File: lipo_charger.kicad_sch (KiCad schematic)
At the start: 19 parts, among them J1 USB_B_Micro, J2 22-23-2021, Q1 2N7002DW-7-F, SW1 SW_SPDT, U1 MCP73831, U2 DIO6605B, U3 AP9101CK

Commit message: Create footprint for boost IC and reroute
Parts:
- U2: footprint Package_DFN_QFN:DFN-8-1EP_3x2mm_P0.5mm_EP1.7x1.4mm -> Package_DFN_QFN:DFN-8-1EP_3x2mm_P0.5mm_EP1.6x1.5mm
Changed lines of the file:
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@@
     (property "Reference" "U2" (id 0) (at 81.28 113.03 0))
     (property "Value" "DIO6605B" (id 1) (at 81.28 115.57 0))
-    (property "Footprint" "Package_DFN_QFN:DFN-8-1EP_3x2mm_P0.5mm_EP1.7x1.4mm" (id 2) (at 71.12 132.08 0)
+    (property "Footprint" "Package_DFN_QFN:DFN-8-1EP_3x2mm_P0.5mm_EP1.6x1.5mm" (id 2) (at 71.12 132.08 0)
       (effects (font (size 1.27 1.27)) hide)
     )
@@
     )
     (path "/850edcd7-b864-48d3-a8a2-fab306866bd1"
-      (reference "U2") (unit 1) (value "DIO6605B") (footprint "Package_DFN_QFN:DFN-8-1EP_3x2mm_P0.5mm_EP1.7x1.4mm")
+      (reference "U2") (unit 1) (value "DIO6605B") (footprint "Package_DFN_QFN:DFN-8-1EP_3x2mm_P0.5mm_EP1.6x1.5mm")
     )
     (path "/72076c21-c88d-4300-b670-44782e8430c6"

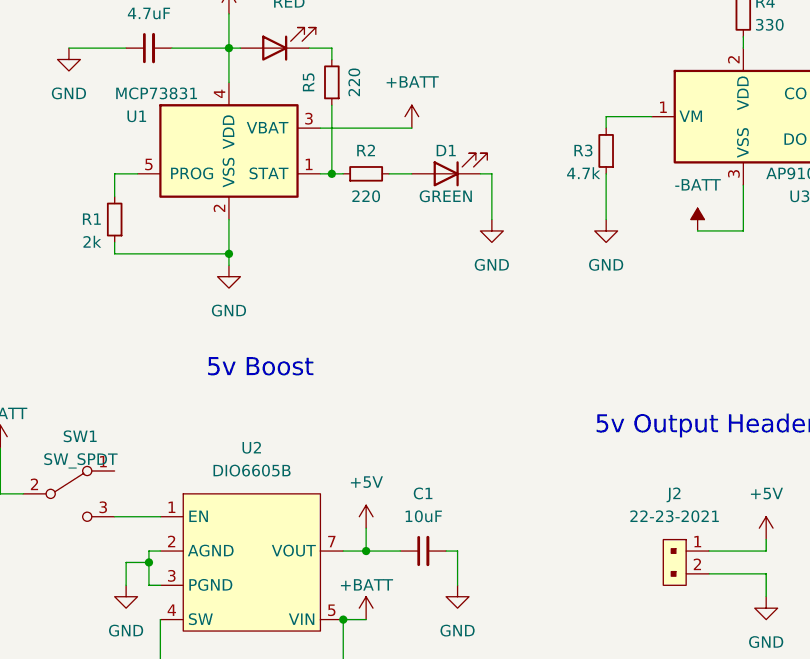
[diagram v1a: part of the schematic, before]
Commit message: Fix incorrect value for R3
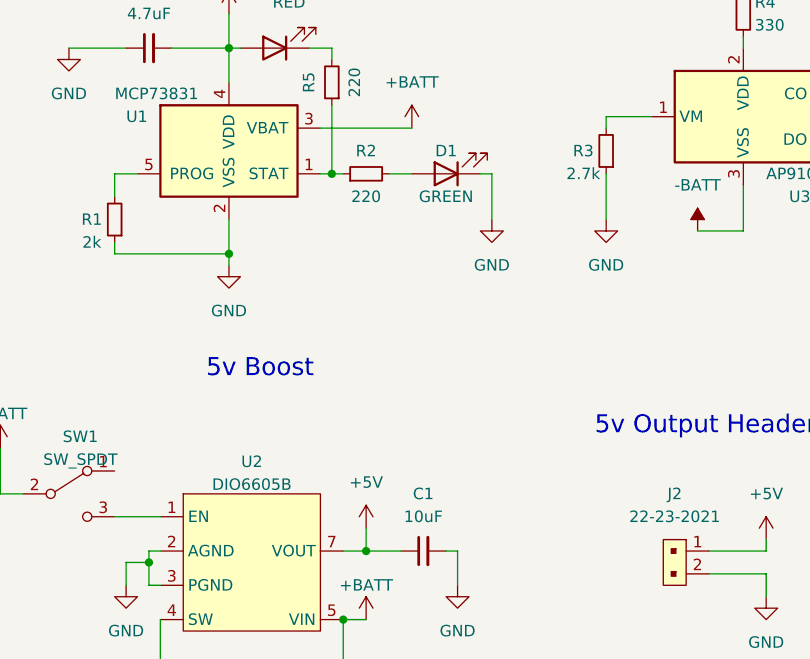
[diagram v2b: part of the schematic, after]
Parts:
- R3: value 4.7k -> 2.7k
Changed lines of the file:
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@@
     (in_bom yes) (on_board yes)
     (property "Reference" "R3" (id 0) (at 118.11 80.01 0))
-    (property "Value" "4.7k" (id 1) (at 118.11 82.55 0))
+    (property "Value" "2.7k" (id 1) (at 118.11 82.55 0))
     (property "Footprint" "Resistor_SMD:R_0805_2012Metric_Pad1.20x1.40mm_HandSolder" (id 2) (at 120.65 80.01 0)
       (effects (font (size 1.27 1.27)) hide)
@@
   (symbol (lib_id "DIO6605BFN8:DIO6605B") (at 81.28 125.73 0) (unit 1)
     (in_bom yes) (on_board yes) (fields_autoplaced)
-    (property "Reference" "U2" (id 0) (at 81.28 113.03 0))
-    (property "Value" "DIO6605B" (id 1) (at 81.28 115.57 0))
+    (property "Reference" "U2" (id 0) (at 81.28 114.5372 0))
+    (property "Value" "DIO6605B" (id 1) (at 81.28 117.0741 0))
     (property "Footprint" "Package_DFN_QFN:DFN-8-1EP_3x2mm_P0.5mm_EP1.6x1.5mm" (id 2) (at 71.12 132.08 0)
       (effects (font (size 1.27 1.27)) hide)
@@
     )
     (path "/56e6188e-bbbc-4aaa-8e4c-89a99b5f65d8"
-      (reference "R3") (unit 1) (value "4.7k") (footprint "Resistor_SMD:R_0805_2012Metric_Pad1.20x1.40mm_HandSolder")
+      (reference "R3") (unit 1) (value "2.7k") (footprint "Resistor_SMD:R_0805_2012Metric_Pad1.20x1.40mm_HandSolder")
     )
     (path "/c2292aaf-d708-456d-8b2c-7fe6a17b8c3e"

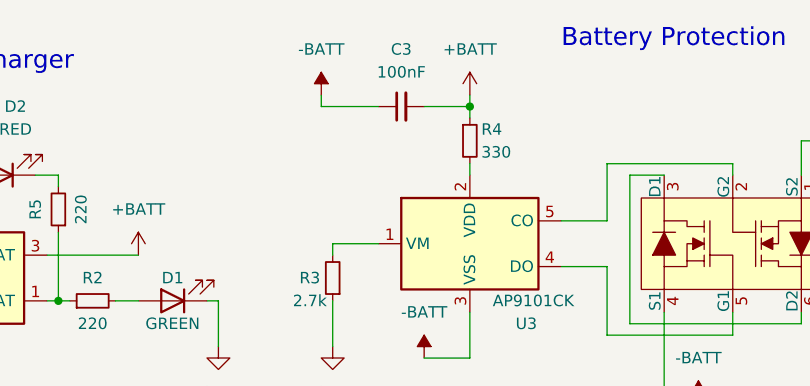
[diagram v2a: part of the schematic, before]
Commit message: Fix misplaced capacitor
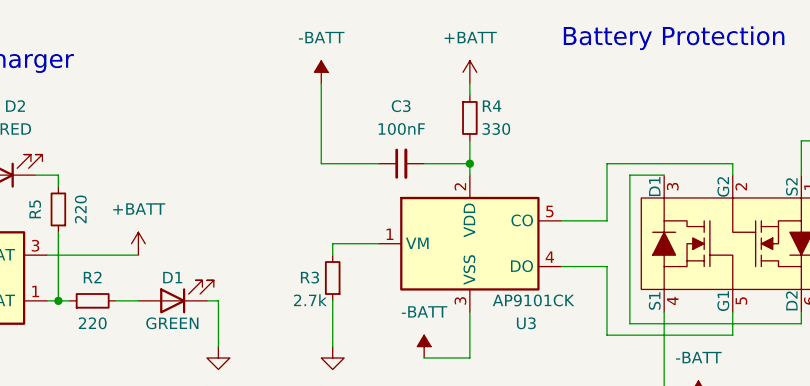
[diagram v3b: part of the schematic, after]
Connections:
- net +BATT: no longer C3.2
- net at R4.2, U3.2 (VDD): now also C3.2
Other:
- moved on the sheet: C3, R4
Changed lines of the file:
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@@
   (junction (at 90.17 82.55) (diameter 0) (color 0 0 0 0)
   )
-  (junction (at 135.89 60.96) (diameter 0) (color 0 0 0 0)
-  )
   (junction (at 78.74 68.58) (diameter 0) (color 0 0 0 0)
   )
   (junction (at 93.98 124.46) (diameter 0) (color 0 0 0 0)
   )
+  (junction (at 135.89 67.31) (diameter 0) (color 0 0 0 0)
+  )
   (junction (at 91.44 132.08) (diameter 0) (color 0 0 0 0)
   )
@@
     (stroke (width 0) (type default) (color 0 0 0 0))
   )
-  (wire (pts (xy 119.38 60.96) (xy 125.73 60.96))
+  (wire (pts (xy 119.38 67.31) (xy 125.73 67.31))
     (stroke (width 0) (type default) (color 0 0 0 0))
   )
@@
     (stroke (width 0) (type default) (color 0 0 0 0))
   )
-  (wire (pts (xy 119.38 59.69) (xy 119.38 60.96))
+  (wire (pts (xy 119.38 58.42) (xy 119.38 67.31))
     (stroke (width 0) (type default) (color 0 0 0 0))
   )
@@
     (stroke (width 0) (type default) (color 0 0 0 0))
   )
+  (wire (pts (xy 135.89 67.31) (xy 135.89 68.58))
+    (stroke (width 0) (type default) (color 0 0 0 0))
+  )
   (wire (pts (xy 22.86 88.9) (xy 29.21 88.9))
     (stroke (width 0) (type default) (color 0 0 0 0))
@@
     (stroke (width 0) (type default) (color 0 0 0 0))
   )
+  (wire (pts (xy 135.89 58.42) (xy 135.89 59.69))
+    (stroke (width 0) (type default) (color 0 0 0 0))
+  )
   (wire (pts (xy 88.9 82.55) (xy 90.17 82.55))
     (stroke (width 0) (type default) (color 0 0 0 0))
   )
-  (wire (pts (xy 135.89 59.69) (xy 135.89 60.96))
-    (stroke (width 0) (type default) (color 0 0 0 0))
-  )
   (wire (pts (xy 71.12 132.08) (xy 71.12 138.43))
     (stroke (width 0) (type default) (color 0 0 0 0))
@@
     (stroke (width 0) (type default) (color 0 0 0 0))
   )
+  (wire (pts (xy 130.81 67.31) (xy 135.89 67.31))
+    (stroke (width 0) (type default) (color 0 0 0 0))
+  )
   (wire (pts (xy 40.64 115.57) (xy 40.64 113.03))
     (stroke (width 0) (type default) (color 0 0 0 0))
@@
     (stroke (width 0) (type default) (color 0 0 0 0))
   )
+  (wire (pts (xy 135.89 64.77) (xy 135.89 67.31))
+    (stroke (width 0) (type default) (color 0 0 0 0))
+  )
   (wire (pts (xy 29.21 85.09) (xy 29.21 88.9))
     (stroke (width 0) (type default) (color 0 0 0 0))
@@
     (stroke (width 0) (type default) (color 0 0 0 0))
   )
-  (wire (pts (xy 130.81 60.96) (xy 135.89 60.96))
-    (stroke (width 0) (type default) (color 0 0 0 0))
-  )
   (wire (pts (xy 66.04 120.65) (xy 71.12 120.65))
     (stroke (width 0) (type default) (color 0 0 0 0))
@@
     (stroke (width 0) (type default) (color 0 0 0 0))
   )
-  (wire (pts (xy 135.89 67.31) (xy 135.89 68.58))
-    (stroke (width 0) (type default) (color 0 0 0 0))
-  )
   (wire (pts (xy 69.85 124.46) (xy 69.85 125.73))
     (stroke (width 0) (type default) (color 0 0 0 0))
@@
   )
   (wire (pts (xy 87.63 68.58) (xy 90.17 68.58))
-    (stroke (width 0) (type default) (color 0 0 0 0))
-  )
-  (wire (pts (xy 135.89 60.96) (xy 135.89 62.23))
     (stroke (width 0) (type default) (color 0 0 0 0))
   )
@@
     (pin "1")
   )
-  (symbol (lib_id "power:-BATT") (at 119.38 59.69 0) (unit 1)
-    (in_bom yes) (on_board yes) (fields_autoplaced)
-    (property "Reference" "#PWR020" (id 0) (at 119.38 63.5 0)
-      (effects (font (size 1.27 1.27)) hide)
-    )
-    (property "Value" "-BATT" (id 1) (at 119.38 54.61 0))
-    (property "Footprint" "" (id 2) (at 119.38 59.69 0)
-      (effects (font (size 1.27 1.27)) hide)
-    )
-    (property "Datasheet" "" (id 3) (at 119.38 59.69 0)
+  (symbol (lib_id "power:-BATT") (at 119.38 58.42 0) (unit 1)
+    (in_bom yes) (on_board yes) (fields_autoplaced)
+    (property "Reference" "#PWR020" (id 0) (at 119.38 62.23 0)
+      (effects (font (size 1.27 1.27)) hide)
+    )
+    (property "Value" "-BATT" (id 1) (at 119.38 53.34 0))
+    (property "Footprint" "" (id 2) (at 119.38 58.42 0)
+      (effects (font (size 1.27 1.27)) hide)
+    )
+    (property "Datasheet" "" (id 3) (at 119.38 58.42 0)
       (effects (font (size 1.27 1.27)) hide)
     )
@@
     (pin "1")
   )
-  (symbol (lib_id "power:+BATT") (at 135.89 59.69 0) (unit 1)
-    (in_bom yes) (on_board yes) (fields_autoplaced)
-    (property "Reference" "#PWR016" (id 0) (at 135.89 63.5 0)
-      (effects (font (size 1.27 1.27)) hide)
-    )
-    (property "Value" "+BATT" (id 1) (at 135.89 54.61 0))
-    (property "Footprint" "" (id 2) (at 135.89 59.69 0)
-      (effects (font (size 1.27 1.27)) hide)
-    )
-    (property "Datasheet" "" (id 3) (at 135.89 59.69 0)
+  (symbol (lib_id "power:+BATT") (at 135.89 58.42 0) (unit 1)
+    (in_bom yes) (on_board yes) (fields_autoplaced)
+    (property "Reference" "#PWR016" (id 0) (at 135.89 62.23 0)
+      (effects (font (size 1.27 1.27)) hide)
+    )
+    (property "Value" "+BATT" (id 1) (at 135.89 53.34 0))
+    (property "Footprint" "" (id 2) (at 135.89 58.42 0)
+      (effects (font (size 1.27 1.27)) hide)
+    )
+    (property "Datasheet" "" (id 3) (at 135.89 58.42 0)
       (effects (font (size 1.27 1.27)) hide)
     )
@@
     (pin "2")
   )
-  (symbol (lib_id "Device:R_Small") (at 135.89 64.77 0) (unit 1)
-    (in_bom yes) (on_board yes)
-    (property "Reference" "R4" (id 0) (at 137.16 63.5 0)
+  (symbol (lib_id "Device:R_Small") (at 135.89 62.23 0) (unit 1)
+    (in_bom yes) (on_board yes)
+    (property "Reference" "R4" (id 0) (at 137.16 60.96 0)
       (effects (font (size 1.27 1.27)) (justify left))
     )
-    (property "Value" "330" (id 1) (at 137.16 66.04 0)
+    (property "Value" "330" (id 1) (at 137.16 63.5 0)
       (effects (font (size 1.27 1.27)) (justify left))
     )
-    (property "Footprint" "Resistor_SMD:R_0805_2012Metric_Pad1.20x1.40mm_HandSolder" (id 2) (at 135.89 64.77 0)
-      (effects (font (size 1.27 1.27)) hide)
-    )
-    (property "Datasheet" "~" (id 3) (at 135.89 64.77 0)
+    (property "Footprint" "Resistor_SMD:R_0805_2012Metric_Pad1.20x1.40mm_HandSolder" (id 2) (at 135.89 62.23 0)
+      (effects (font (size 1.27 1.27)) hide)
+    )
+    (property "Datasheet" "~" (id 3) (at 135.89 62.23 0)
       (effects (font (size 1.27 1.27)) hide)
     )
@@
     (pin "2")
   )
-  (symbol (lib_id "Device:C_Small") (at 128.27 60.96 90) (unit 1)
-    (in_bom yes) (on_board yes) (fields_autoplaced)
-    (property "Reference" "C3" (id 0) (at 128.2763 54.61 90))
-    (property "Value" "100nF" (id 1) (at 128.2763 57.15 90))
-    (property "Footprint" "Capacitor_SMD:C_0805_2012Metric" (id 2) (at 128.27 60.96 0)
-      (effects (font (size 1.27 1.27)) hide)
-    )
-    (property "Datasheet" "~" (id 3) (at 128.27 60.96 0)
-      (effects (font (size 1.27 1.27)) hide)
-    )
+  (symbol (lib_id "Device:C_Small") (at 128.27 67.31 90) (unit 1)
+    (in_bom yes) (on_board yes) (fields_autoplaced)
+    (property "Reference" "C3" (id 0) (at 128.2763 60.96 90))
+    (property "Value" "100nF" (id 1) (at 128.2763 63.5 90))
+    (property "Footprint" "Capacitor_SMD:C_0805_2012Metric" (id 2) (at 128.27 67.31 0)
+      (effects (font (size 1.27 1.27)) hide)
+    )
+    (property "Datasheet" "~" (id 3) (at 128.27 67.31 0)
+      (effects (font (size 1.27 1.27)) hide)
+    )
